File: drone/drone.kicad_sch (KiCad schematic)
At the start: 51 parts, among them J2 HMC5883, J3 Conn_01x03_Pin, Q1 AO3400A, U2 MPU-6050, U3 MP2303ADN

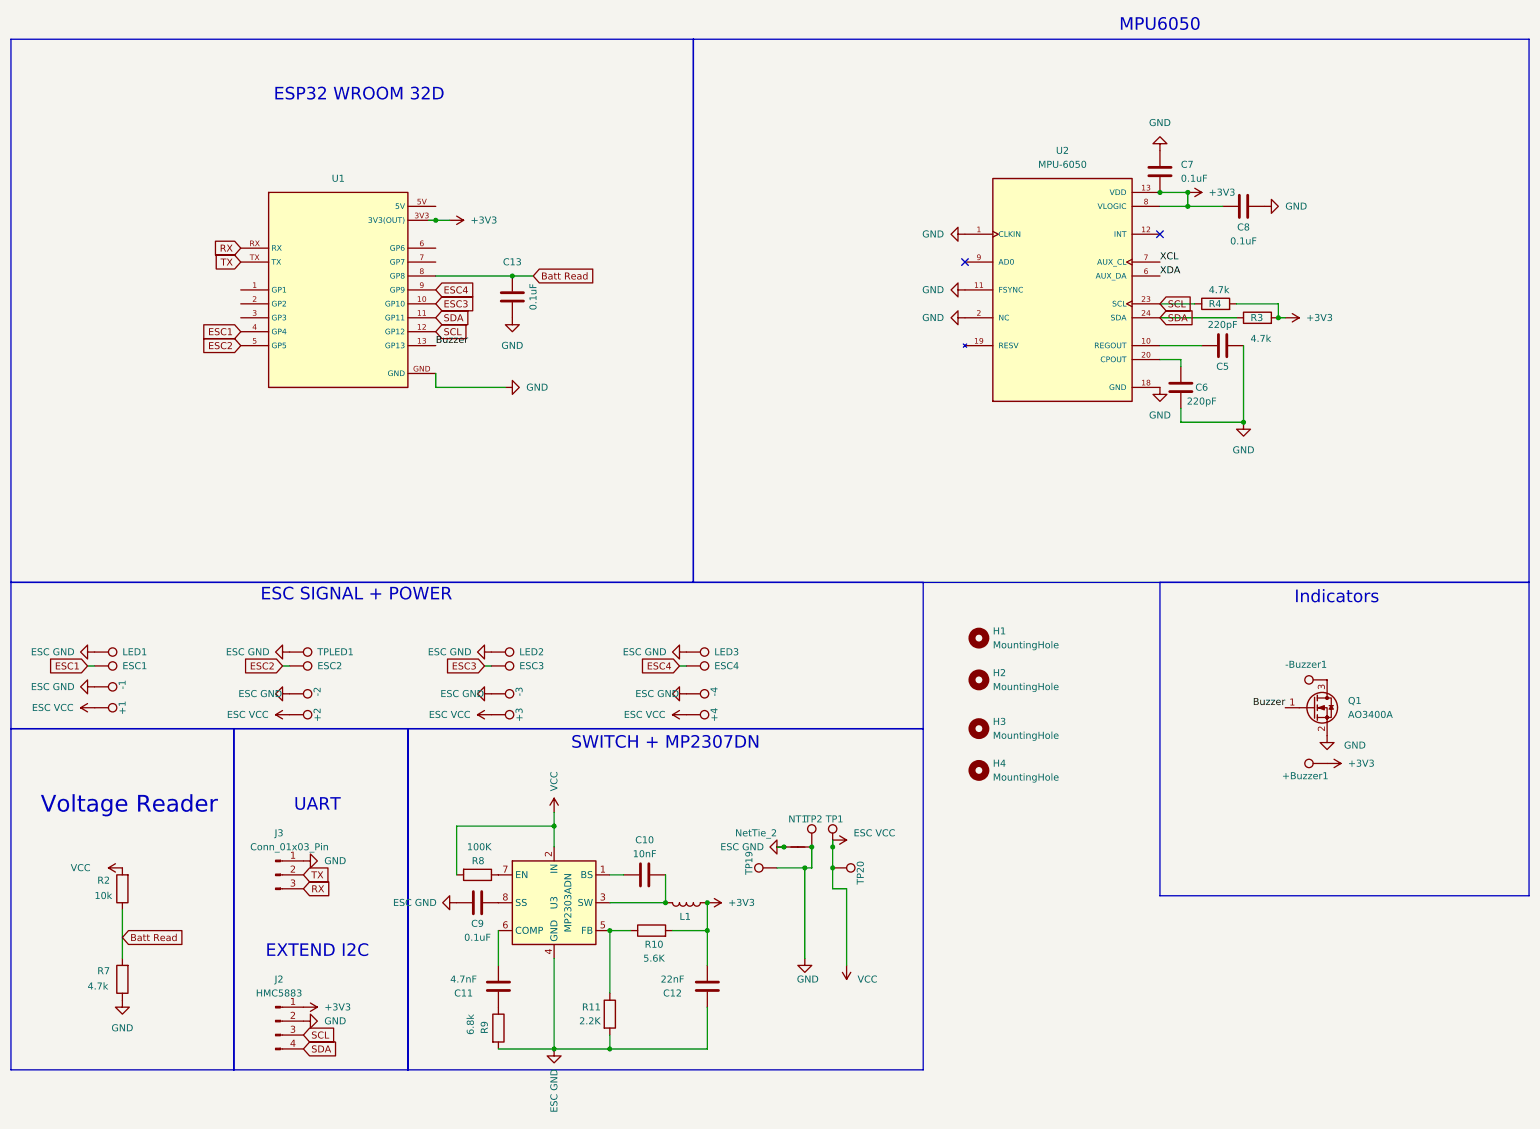
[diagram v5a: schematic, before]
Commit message: silk + external uart + i2c
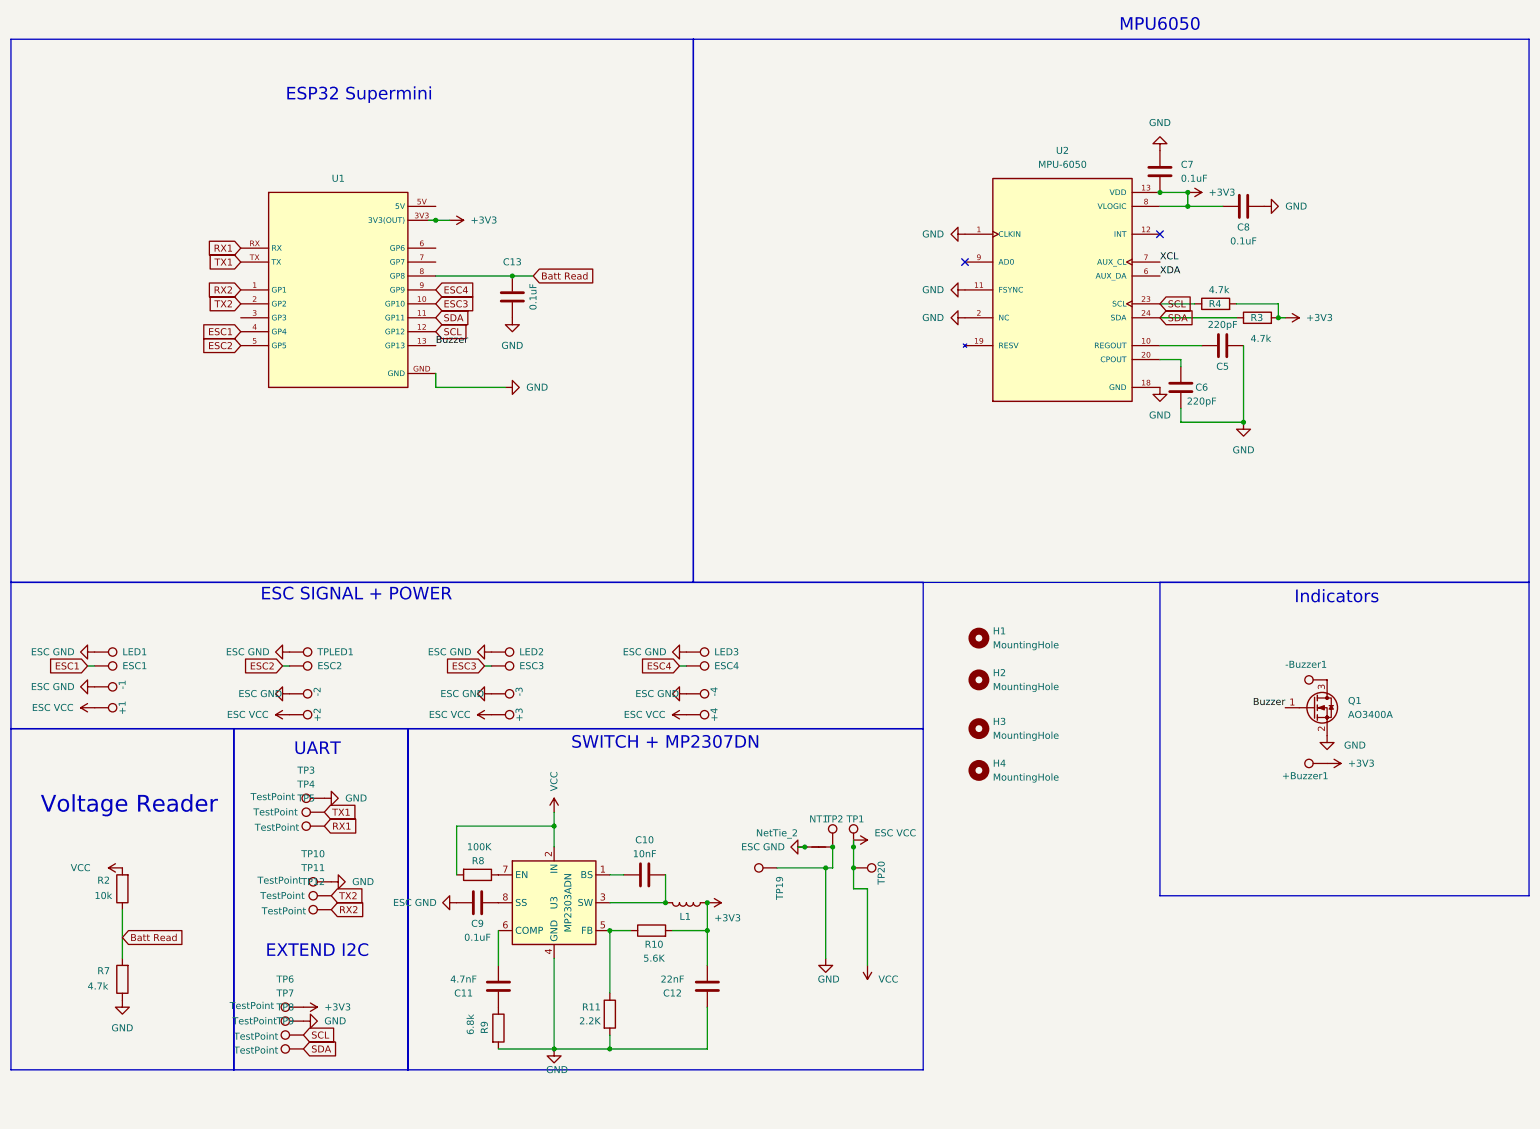
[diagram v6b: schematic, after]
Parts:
- removed J2: HMC5883, symbol Connector:Conn_01x04_Pin
- removed J3: Conn_01x03_Pin, Connector_PinHeader_2.54mm:PinHeader_1x03_P2.54mm_Vertical, symbol Connector:Conn_01x03_Pin
- added TP10, TP11, TP12, TP3, TP4, TP5, TP6, TP7, TP8, TP9: TestPoint, TestPoint:TestPoint_Pad_D1.0mm, symbol Connector:TestPoint
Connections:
- net +3V3: now also TP6.1
- net ESC GND: no longer C12.2, R11.2, R9.2, U3.4 (GND)
- net GND: now also C12.2, R11.2, R9.2, U3.4 (GND), TP10.1, TP3.1, TP7.1
- net SCL: now also TP8.1
- net SDA: now also TP9.1
- net RX2: now reaches U1.1 (GP1)
- net RX2: now also TP12.1
- net TX2: now reaches U1.2 (GP2)
- net TX2: now also TP11.1
- net RX renamed RX1
- net RX1: now also TP5.1
- net TX renamed TX1
- net TX1: now also TP4.1
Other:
- note added: "ESP32 Supermini"
- note removed: "ESP32 WROOM 32D"
- moved on the sheet: NT1, TP1, TP2, TP20

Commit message: hi
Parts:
- R10: value 5.6K -> 22K
- R11: value 2.2K -> 4.7K
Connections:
- net +3V3: no longer C12.1, L1.1, R10.2
- net ESC1: now also U1.6 (GP6); no longer U1.4 (GP4)
- net ESC2: now also U1.7 (GP7); no longer U1.5 (GP5)
- net +5V: now reaches U1.5V
- net +5V: now also C12.1, L1.1, R10.2
